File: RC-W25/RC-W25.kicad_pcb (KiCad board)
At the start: 2 copper layers, 48 parts, among them J1 USB_C_Receptacle_USB2.0_14P, P1 JST CONN, P2 JST CONN, Q1 NMOS, U1 ESP32-C6-WROOM-1, U2 MCP73831-5-OT, U3 AP62300TWU, U4 TMAG5253

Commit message: EM Custom RC V1
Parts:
- added H1: MountingHole, MountingHole:MountingHole_2.2mm_M2, F.Cu at (123.3, 114.5)
- added H2: MountingHole, MountingHole:MountingHole_2.2mm_M2, F.Cu at (157.0, 135.7)
- added H3: MountingHole, MountingHole:MountingHole_2.2mm_M2, F.Cu at (156.8, 63.6)
- added H4: MountingHole, MountingHole:MountingHole_2.2mm_M2, F.Cu at (123.7, 63.6)
- added SW1: Button, footprints:SW-SMD_L3.9-W3.0-P4.45, F.Cu at (130.5, 153.2)
- added SW2: Button, footprints:SW-SMD_L3.9-W3.0-P4.45, F.Cu at (140.3, 141.7)
- added SW4: Button, footprints:SW-SMD_L3.9-W3.0-P4.45, F.Cu at (151.3, 71.9)
- added SW5: YTSPS-22E58LM, footprints:SW-SMD_6P-YTSPS-22E58LM, F.Cu at (154.8, 144.7)
- moved R7 29.2 mm to (132.8, 151.2)
- moved U3 27.1 mm to (145.4, 132.0)
- moved R8 27.1 mm to (133.9, 151.1)
- moved J1 27.0 mm to (139.9, 156.2)
- moved C2 27.0 mm to (146.4, 114.2)
- moved C5 27.0 mm to (131.4, 149.2)
- moved C9 27.0 mm to (134.8, 132.8)
- moved D2 27.0 mm to (137.1, 150.8)
- moved P1 27.0 mm to (154.8, 152.7)
- moved R2 27.0 mm to (141.8, 149.7)
- moved R3 27.0 mm to (140.8, 114.2)
- moved C1 27.0 mm to (147.8, 114.2)
- moved C3 27.0 mm to (133.3, 114.2)
- moved C4 27.0 mm to (135.3, 114.2)
- moved D5 27.0 mm to (133.2, 74.0)
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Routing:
- net +VBAT: track 3.57 -> 130.1 mm
- net +3.3V: track 40.3 -> 148.3 mm, vias 0 -> 2
- net GPIO_MODE: track 0.00 -> 80.4 mm
- net GPIO_EN1: track 102.8 -> 83.4 mm
- net ADC_BATTERYPERCENT: track 38.7 -> 26.9 mm
- net +USB5V: track 37.5 -> 45.4 mm
- net ADC_HALLEFFECT1: track 92.0 -> 84.9 mm
- net Net-(D5-A): track 6.44 -> 0.00 mm
- net Net-(P1-Pin_1): track 15.9 -> 21.5 mm
- net GPIO_RUMBLE_CNTL: track 72.7 -> 68.8 mm, vias 0 -> 2
- net GND: track 59.7 -> 63.4 mm, vias 35 -> 40
- net Net-(R15-Pad2): track 0.00 -> 3.01 mm
- net /RC_Connections/RESET: track 4.78 -> 7.65 mm
- net USB_D+: track 12.8 -> 15.1 mm
- net /RC_Connections/FLASH: track 0.00 -> 2.02 mm
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- added copper zone on B.Cu, net GND
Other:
- board outline added: 40.3 x 100 mm
- board text removed: "switch here"

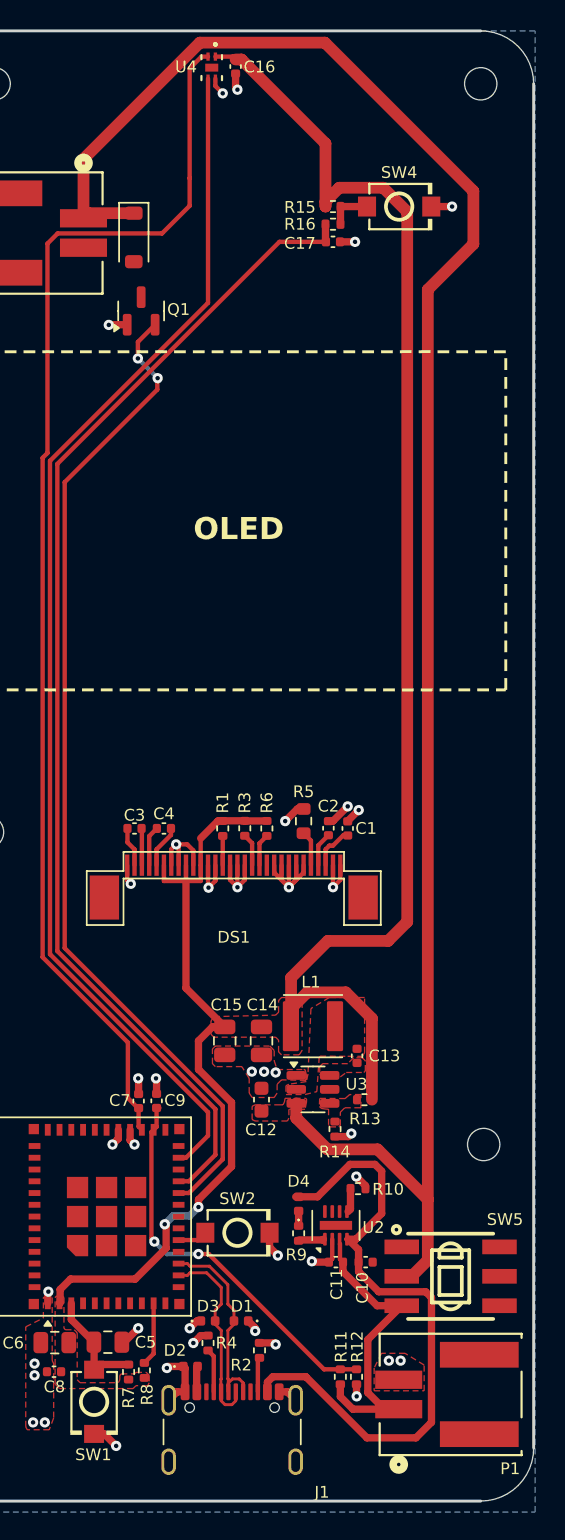
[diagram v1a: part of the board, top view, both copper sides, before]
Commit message: em crc v1
remaining tasks:

- clean up + verify
- potentially try to lose the 3 via jumps
- spec out jst connectors
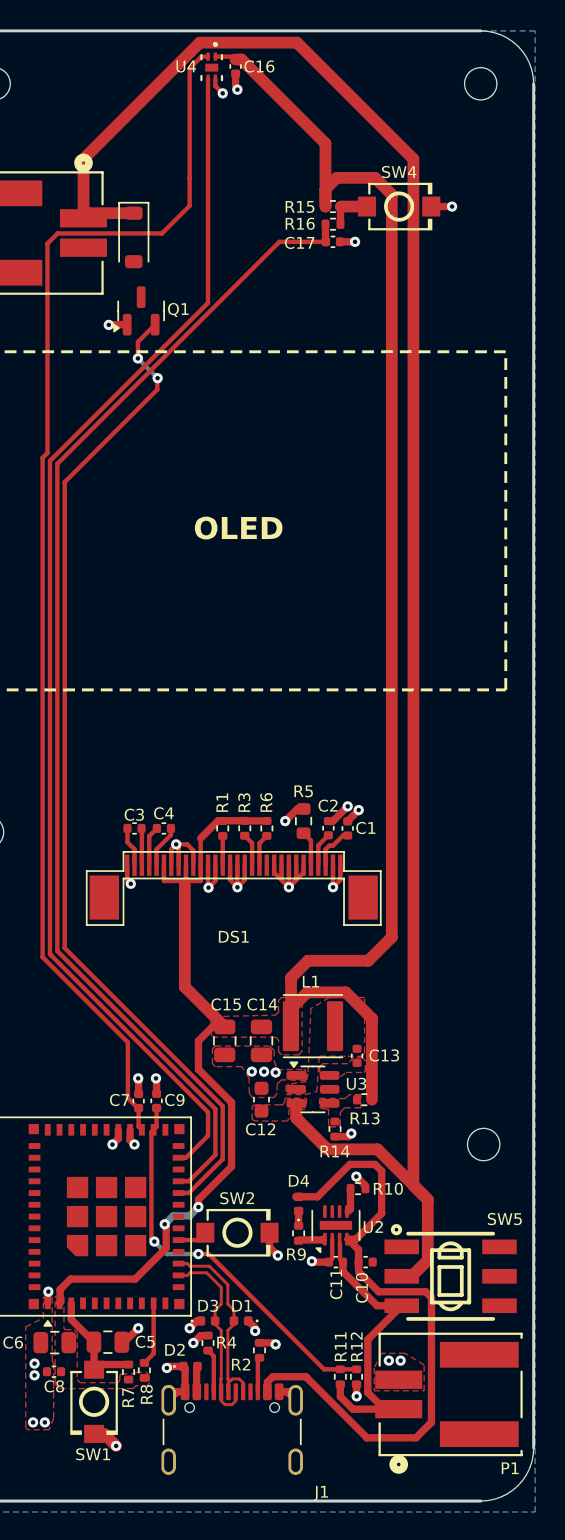
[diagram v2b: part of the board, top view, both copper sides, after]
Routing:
- net +VBAT: track 130.1 -> 126.4 mm

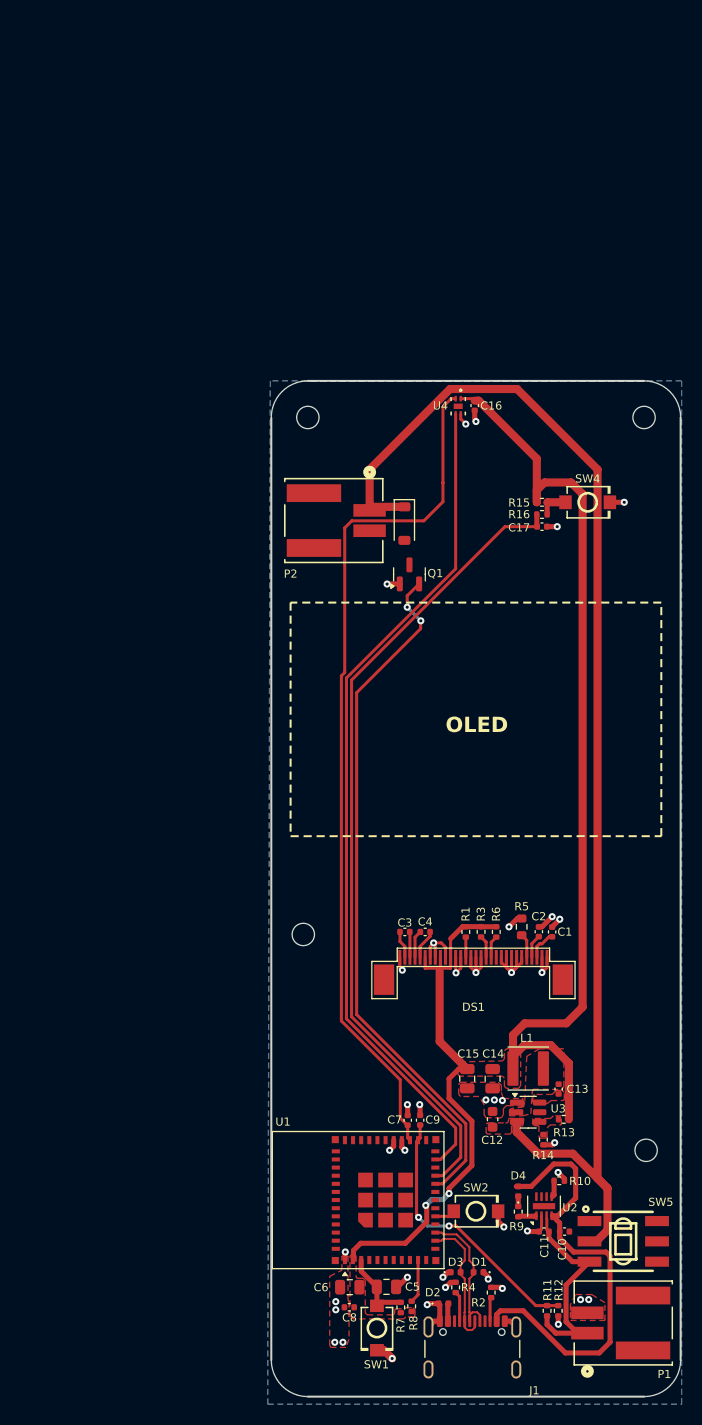
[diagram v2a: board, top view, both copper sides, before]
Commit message: crc v1
finalized!! finally!! yes!!

- spec out 3.7V 1000mAh cell
- spec out ultra-thin coin motor

^make sure they have a jst-ph male connector or are organized to be ordered alongside one for manual soldering.
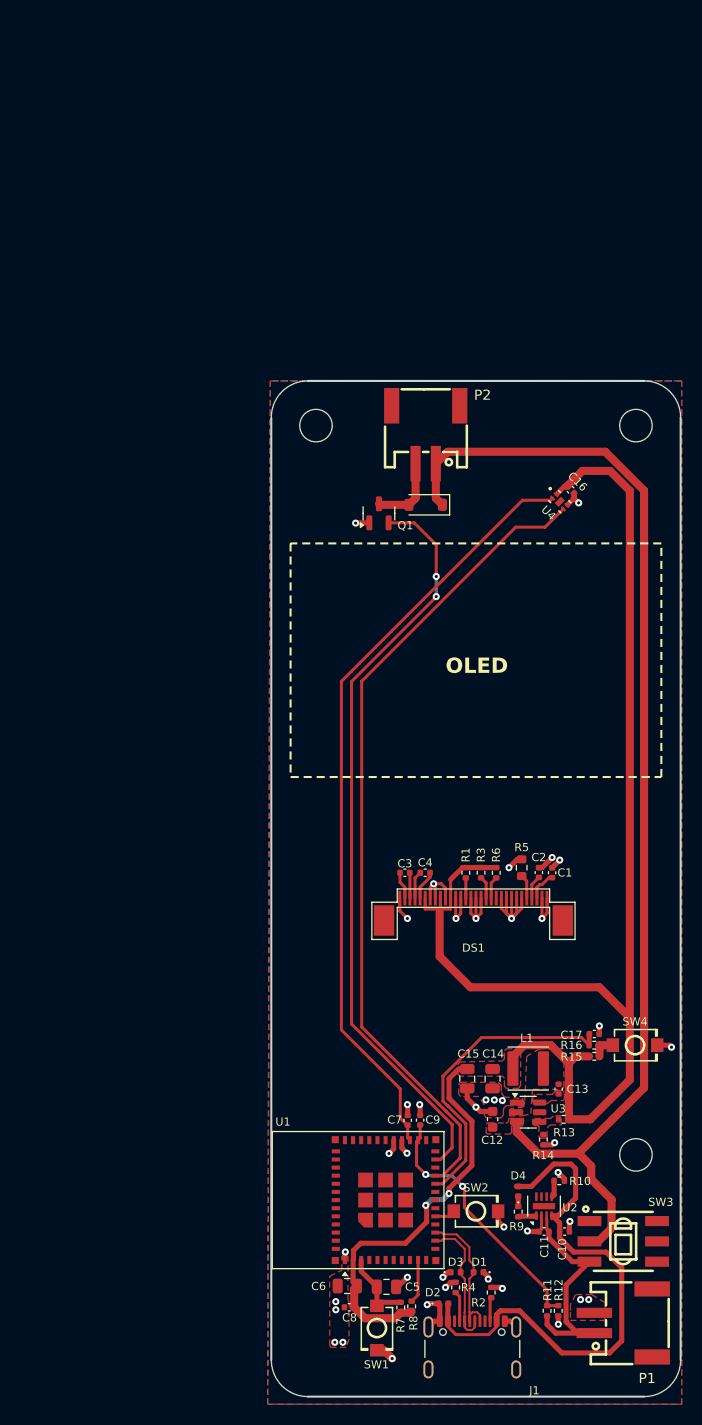
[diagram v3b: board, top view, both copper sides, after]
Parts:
- removed the H1 at (123.3, 114.5)
- H1: renamed from H2; footprint MountingHole:MountingHole_2.2mm_M2 -> MountingHole:MountingHole_3.2mm_M3
- H2: renamed from H3; footprint MountingHole:MountingHole_2.2mm_M2 -> MountingHole:MountingHole_3.2mm_M3
- H3: renamed from H4; footprint MountingHole:MountingHole_2.2mm_M2 -> MountingHole:MountingHole_3.2mm_M3
- P1, P2: footprint Library:CONN02_502352_MOL -> footprints:CONN-SMD_2P-P2.00_XUNPU_WAFER-PH2.0-2PWB
- moved R15 54.8 mm to (151.9, 126.5)
- moved SW4 53.7 mm to (155.9, 125.4)
- moved R16 52.5 mm to (151.9, 125.4)
- moved C17 50.2 mm to (151.9, 124.3)
- moved U4 13.7 mm to (148.5, 71.9), turned to -45 degrees
- moved C16 12.6 mm to (149.6, 70.7), turned to -45 degrees
- moved P2 12.4 mm to (135.3, 65.3), turned to 180 degrees
- moved Q1 6.72 mm to (130.7, 73.0)
- moved C1 5.82 mm to (147.8, 108.4)
- moved C2 5.82 mm to (146.4, 108.4)
- moved C3 5.82 mm to (133.3, 108.4)
- moved C4 5.82 mm to (135.3, 108.4)
- moved DS1 5.82 mm to (140.0, 110.9)
- moved R1 5.82 mm to (139.3, 108.4)
- moved R3 5.82 mm to (140.8, 108.4)
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- renumbered SW5 to SW3
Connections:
- U1 pad 20: GPIO_RUMBLE_CNTL -> GPIO_MODE
- U1 pad 21: GPIO_MODE -> GPIO_EN1
- U1 pad 23: GPIO_EN1 -> GPIO_RUMBLE_CNTL
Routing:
- net GPIO_MODE: track 80.4 -> 30.6 mm
- net +3.3V: track 148.4 -> 168.8 mm
- net GND: track 63.4 -> 76.2 mm, vias 40 -> 41
- net +VBAT: track 126.4 -> 114.0 mm
- net ADC_HALLEFFECT1: track 84.9 -> 76.3 mm
- net +USB5V: track 45.4 -> 53.5 mm
- net Net-(D5-A): track 0.00 -> 7.31 mm
- net GPIO_RUMBLE_CNTL: track 68.8 -> 74.6 mm
- net GPIO_EN1: track 83.4 -> 81.0 mm
- net ADC_BATTERYPERCENT: track 26.9 -> 26.0 mm

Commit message: crc v1
board complete and ready for assembly setup!
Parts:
- C5: value 1uF -> 100nF; footprint Capacitor_SMD:C_0805_2012Metric -> Capacitor_SMD:C_0402_1005Metric; moved to B.Cu
- C6: value 22uF -> 100nF; footprint Capacitor_SMD:C_0805_2012Metric -> Capacitor_SMD:C_0402_1005Metric; moved to B.Cu
- C7, C9, R7: moved to B.Cu
- C8: value 100nF -> 22uF; footprint Capacitor_SMD:C_0402_1005Metric -> Capacitor_SMD:C_0805_2012Metric; moved to B.Cu
- U1: value ESP32-C6-WROOM-1 -> ESP32-C6-MINI-1; moved to B.Cu
- moved H1 107.3 mm to (137.5, 30.5)
- moved P1 77.0 mm to (119.6, 84.2), turned to -90 degrees
- moved R11 71.3 mm to (125.8, 83.6), turned to 180 degrees
- moved R12 70.6 mm to (125.8, 84.7), turned to 0 degrees
- moved SW1 62.3 mm to (126.9, 91.1), turned to 0 degrees
- moved P2 57.2 mm to (119.5, 120.2), turned to 0 degrees
- moved H2 55.1 mm to (112.5, 30.5)
- moved SW3 54.0 mm to (134.2, 94.8), turned to 90 degrees
- moved SW2 47.9 mm to (126.8, 95.8)
- moved SW4 47.5 mm to (135.8, 82.4), turned to 90 degrees
- moved D5 45.4 mm to (117.5, 114.0), turned to 0 degrees
- moved R8 45.1 mm to (126.2, 106.7), turned to -90 degrees
- moved R15 43.7 mm to (134.6, 86.4), turned to 90 degrees
- moved R16 42.2 mm to (135.8, 86.4), turned to -90 degrees
- moved C1 41.5 mm to (132.0, 70.0)
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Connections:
- C5 pad 1: /RC_Connections/RESET -> ADC_HALLEFFECT1
- C6 pad 1: +3.3V -> /RC_Connections/RESET
- C7 pad 1: ADC_HALLEFFECT1 -> ADC_BATTERYPERCENT
- C9 pad 1: ADC_BATTERYPERCENT -> +3.3V
- R8 pad 2: Net-(U1-GPIO8) -> Net-(U1-IO8)
- U1 pad 10: Net-(U1-GPIO8) -> unconnected-(U1-IO5-Pad10)
- U1 pad 11: unconnected-(U1-GPIO10-Pad11) -> GND
- U1 pad 12: unconnected-(U1-GPIO11-Pad12) -> GND
- U1 pad 13: USB_D- -> GND
- U1 pad 14: USB_D+ -> GND
- U1 pad 16: /RC_Connections/FLASH -> unconnected-(U1-IO7-Pad16)
- U1 pad 17: unconnected-(U1-GPIO19-Pad17) -> USB_D-
- U1 pad 18: unconnected-(U1-GPIO20-Pad18) -> USB_D+
- U1 pad 2: +3.3V -> GND
- U1 pad 20: GPIO_MODE -> unconnected-(U1-IO15-Pad20)
- U1 pad 21: GPIO_EN1 -> unconnected-(U1-NC-Pad21)
- U1 pad 22: unconnected-(U1-NC-Pad22) -> Net-(U1-IO8)
- U1 pad 23: GPIO_RUMBLE_CNTL -> /RC_Connections/FLASH
- U1 pad 26: ADC_BATTERYPERCENT -> unconnected-(U1-IO20-Pad26)
- U1 pad 27: ADC_HALLEFFECT1 -> unconnected-(U1-IO21-Pad27)
- U1 pad 28: GND -> GPIO_EN1
- U1 pad 29: GND -> unconnected-(U1-IO23-Pad29)
- U1 pad 3: /RC_Connections/RESET -> +3.3V
- U1 pad 30: (no net) -> unconnected-(U1-RXD0-Pad30)
- U1 pad 31: (no net) -> unconnected-(U1-TXD0-Pad31)
- U1 pad 32: (no net) -> unconnected-(U1-NC-Pad32)
- U1 pad 33: (no net) -> unconnected-(U1-NC-Pad33)
- U1 pad 34: (no net) -> unconnected-(U1-NC-Pad34)
- U1 pad 35: (no net) -> unconnected-(U1-NC-Pad35)
- U1 pad 36: (no net) -> GND
- U1 pad 37: (no net) -> GND
- U1 pad 38: (no net) -> GND
- U1 pad 39: (no net) -> GND
- U1 pad 40: (no net) -> GND
- U1 pad 41: (no net) -> GND
- U1 pad 42: (no net) -> GND
- U1 pad 43: (no net) -> GND
- U1 pad 44: (no net) -> GND
- U1 pad 45: (no net) -> GND
- U1 pad 46: (no net) -> GND
- U1 pad 47: (no net) -> GND
- U1 pad 48: (no net) -> GND
- U1 pad 49: (no net) -> GND
- U1 pad 5: unconnected-(U1-MTDI/GPIO5/ADC1_CH5-Pad5) -> ADC_HALLEFFECT1
- U1 pad 50: (no net) -> GND
- U1 pad 51: (no net) -> GND
- U1 pad 52: (no net) -> GND
- U1 pad 53: (no net) -> GND
- U1 pad 6: unconnected-(U1-MTCK/GPIO6/ADC1_CH6-Pad6) -> ADC_BATTERYPERCENT
- U1 pad 8: unconnected-(U1-GPIO0/ADC1_CH0/XTAL_32K_P-Pad8) -> /RC_Connections/RESET
- U1 pad 9: unconnected-(U1-GPIO1/ADC1_CH1/XTAL_32K_N-Pad9) -> GPIO_MODE
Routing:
- net GPIO_RUMBLE_CNTL: track 74.6 -> 0.00 mm, vias 2 -> 0
- net +VBAT: track 114.0 -> 42.0 mm
- net GND: track 76.2 -> 19.9 mm, vias 41 -> 256
- net /RC_Connections/RESET: track 7.65 -> 33.2 mm, vias 0 -> 1
- net Net-(P1-Pin_1): track 21.5 -> 45.4 mm
- net +USB5V: track 53.5 -> 32.4 mm
- net ADC_BATTERYPERCENT: track 26.0 -> 41.2 mm, vias 2 -> 1
- net GPIO_MODE: track 30.6 -> 42.6 mm, vias 0 -> 1
- net +3.3V: track 168.8 -> 180.3 mm, vias 2 -> 1
- net GPIO_EN1: track 81.0 -> 71.1 mm, vias 0 -> 1
- net Net-(U3-SW): track 0.00 -> 7.85 mm
- net /RC_Connections/FLASH: track 2.02 -> 9.16 mm, vias 0 -> 1
- net ADC_HALLEFFECT1: track 76.3 -> 82.8 mm, vias 0 -> 1
- net Net-(U1-IO8): track 0.00 -> 5.04 mm, vias 0 -> 1
- net Net-(U1-GPIO8): track 4.31 -> 0.00 mm
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- added copper zone on B.Cu, net +3.3V
- added copper zone on F.Cu, net Net-(R15-Pad2)
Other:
- board size 40.3 x 100 mm -> 36 x 100.1 mm

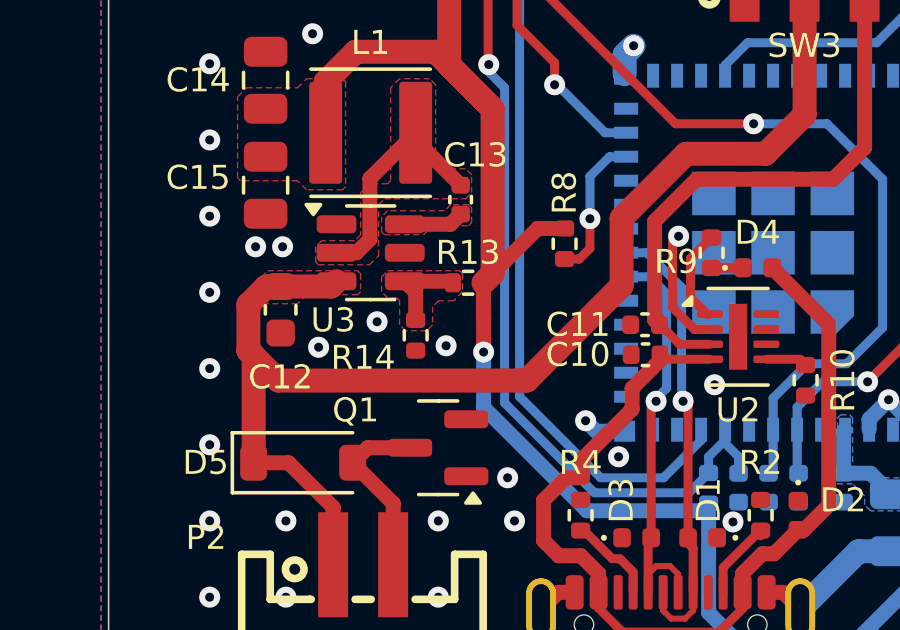
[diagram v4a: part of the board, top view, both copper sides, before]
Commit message: crc v1
board complete and ready for assembly setup
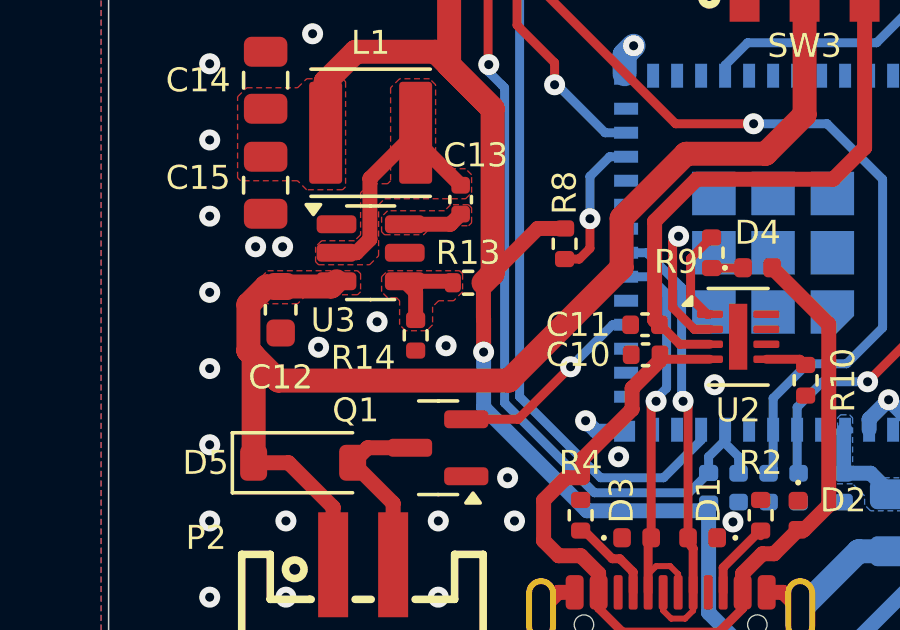
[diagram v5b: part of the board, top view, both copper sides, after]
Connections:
- U1 pad 15: unconnected-(U1-IO6-Pad15) -> GPIO_RUMBLE_CNTL
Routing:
- net GPIO_RUMBLE_CNTL: track 0.00 -> 6.63 mm, vias 0 -> 1

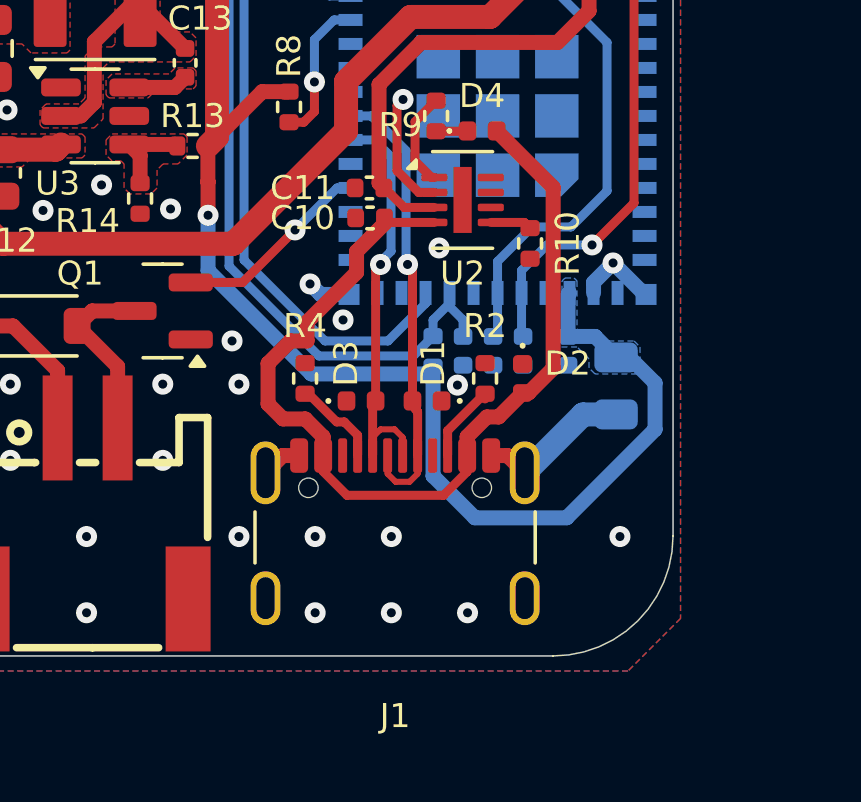
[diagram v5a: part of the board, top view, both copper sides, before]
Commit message: crc v1
board finished and ready for assembly setup!
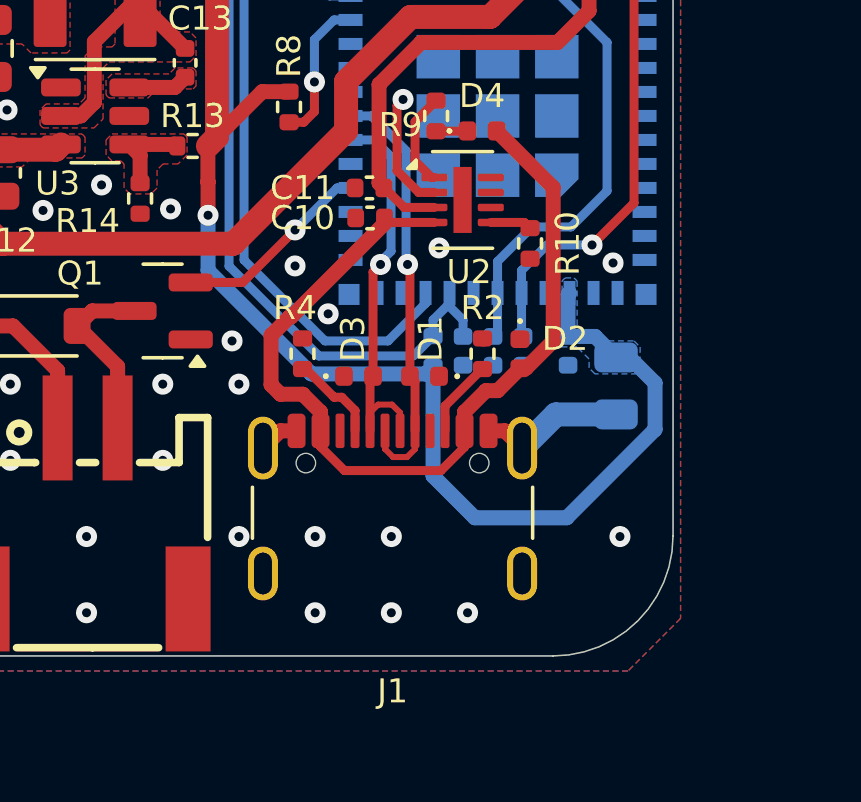
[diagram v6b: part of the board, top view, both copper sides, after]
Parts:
- moved D1 0.83 mm to (130.7, 115.7)
- moved D2 0.83 mm to (133.9, 114.9)
- moved D3 0.83 mm to (128.5, 115.7)
- moved J1 0.83 mm to (129.7, 121.2)
- moved R2 0.83 mm to (132.7, 114.9)
- moved R4 0.83 mm to (126.7, 114.9)
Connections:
- U1 pad 12: GND -> unconnected-(U1-IO0-Pad12)
- U1 pad 13: GND -> unconnected-(U1-IO1-Pad13)
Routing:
- net GND: track 19.9 -> 15.5 mm, vias 256 -> 255
- net +USB5V: track 32.4 -> 30.4 mm
- net USB_D-: track 14.2 -> 13.4 mm
- net USB_D+: track 14.8 -> 14.2 mm
